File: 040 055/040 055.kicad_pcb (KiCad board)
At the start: 2 copper layers, 25.6 x 21.5 mm, 10 parts, among them J1 USB, J2 040, J3 05X

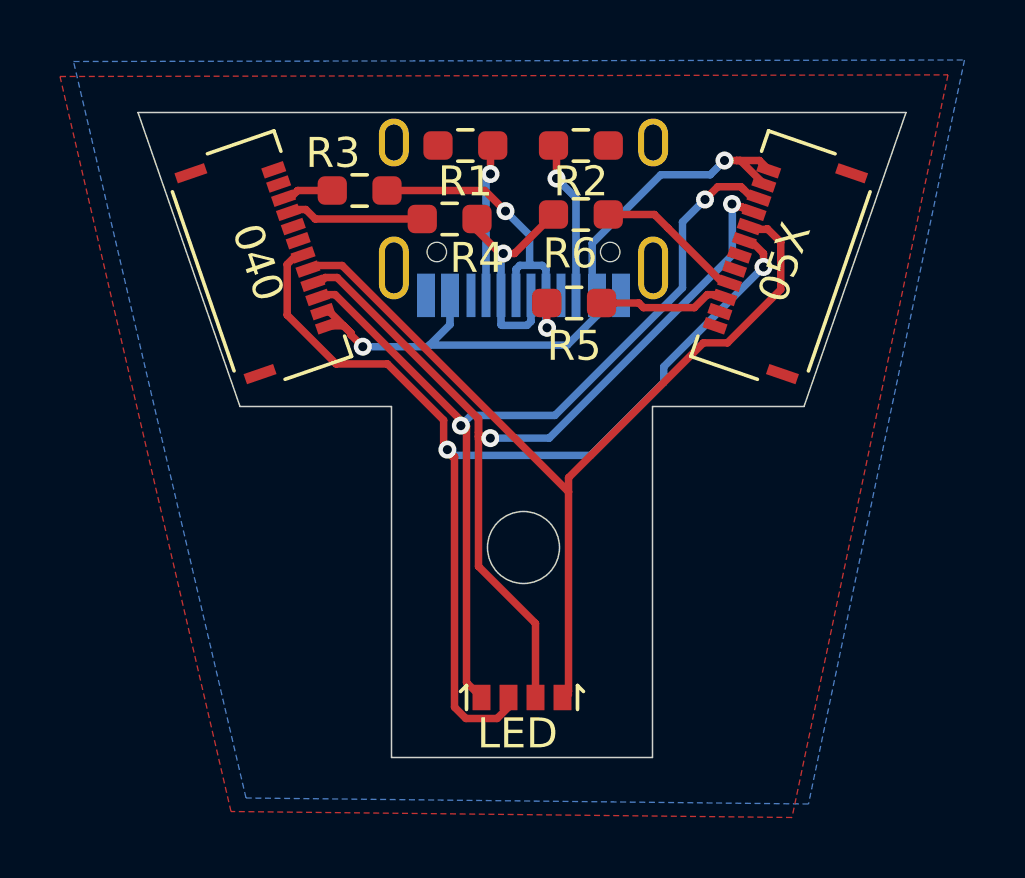
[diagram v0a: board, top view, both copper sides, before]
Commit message: Update 030 and 040 055 board to include screw mounting holes
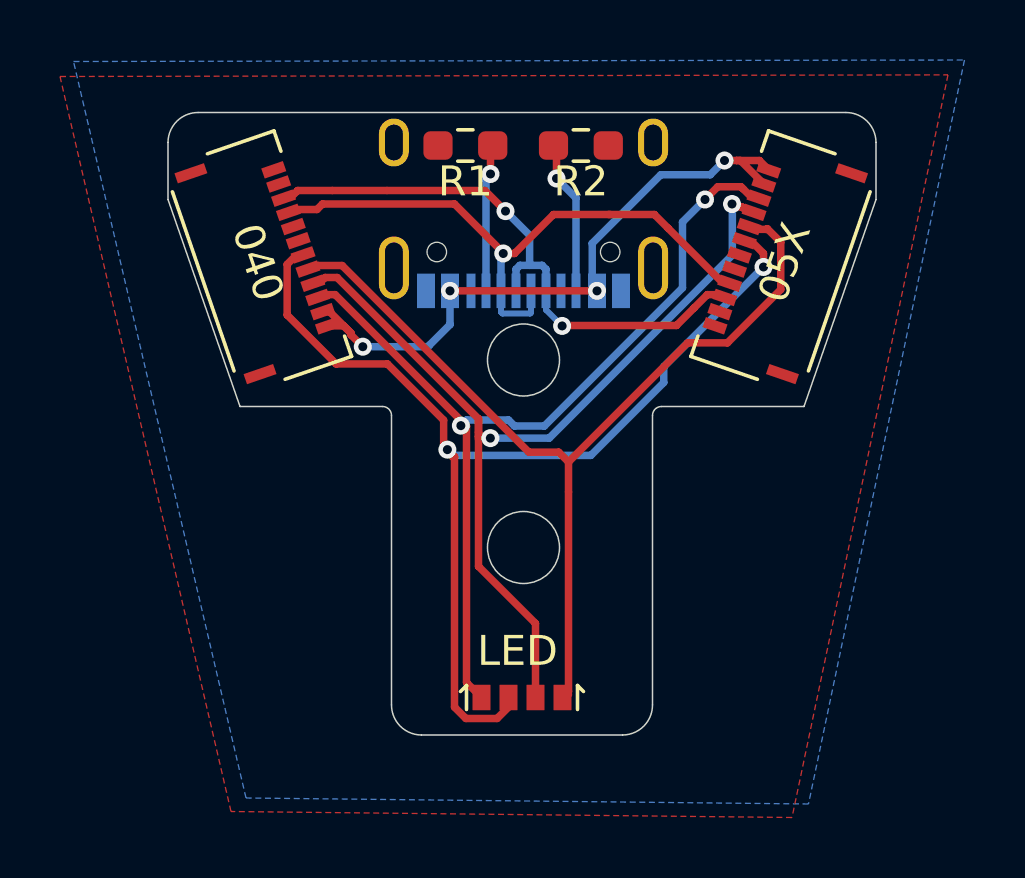
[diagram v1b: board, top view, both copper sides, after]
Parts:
- removed R3, R4, R5, R6: Comp, Resistor_SMD:R_0603_1608Metric_Pad0.98x0.95mm_HandSolder
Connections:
- J2 pad 13: (no net) -> GND
- J2 pad 14: (no net) -> GND
- J3 pad 13: (no net) -> GND
- J3 pad 14: (no net) -> GND
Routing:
- net Net-(J2-Pad4): track 4.28 -> 7.56 mm
- net Net-(J2-Pad3): track 1.38 -> 3.21 mm
- net /vcc: track 23.8 -> 22.0 mm, vias 2 -> 4
- net Net-(J3-Pad3): track 4.04 -> 5.53 mm
- net /d+: track 11.2 -> 10.6 mm
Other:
- board size 25.6 x 21.5 mm -> 23.6 x 20.8 mm
- net class Default removed
- board text added: "JDS-040/055 Replacement"
